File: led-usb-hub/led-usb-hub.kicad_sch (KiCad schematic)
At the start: 9 parts, among them J1 USB_C_Receptacle_USB2.0, U1 SL2.1A, Y1 12MHz

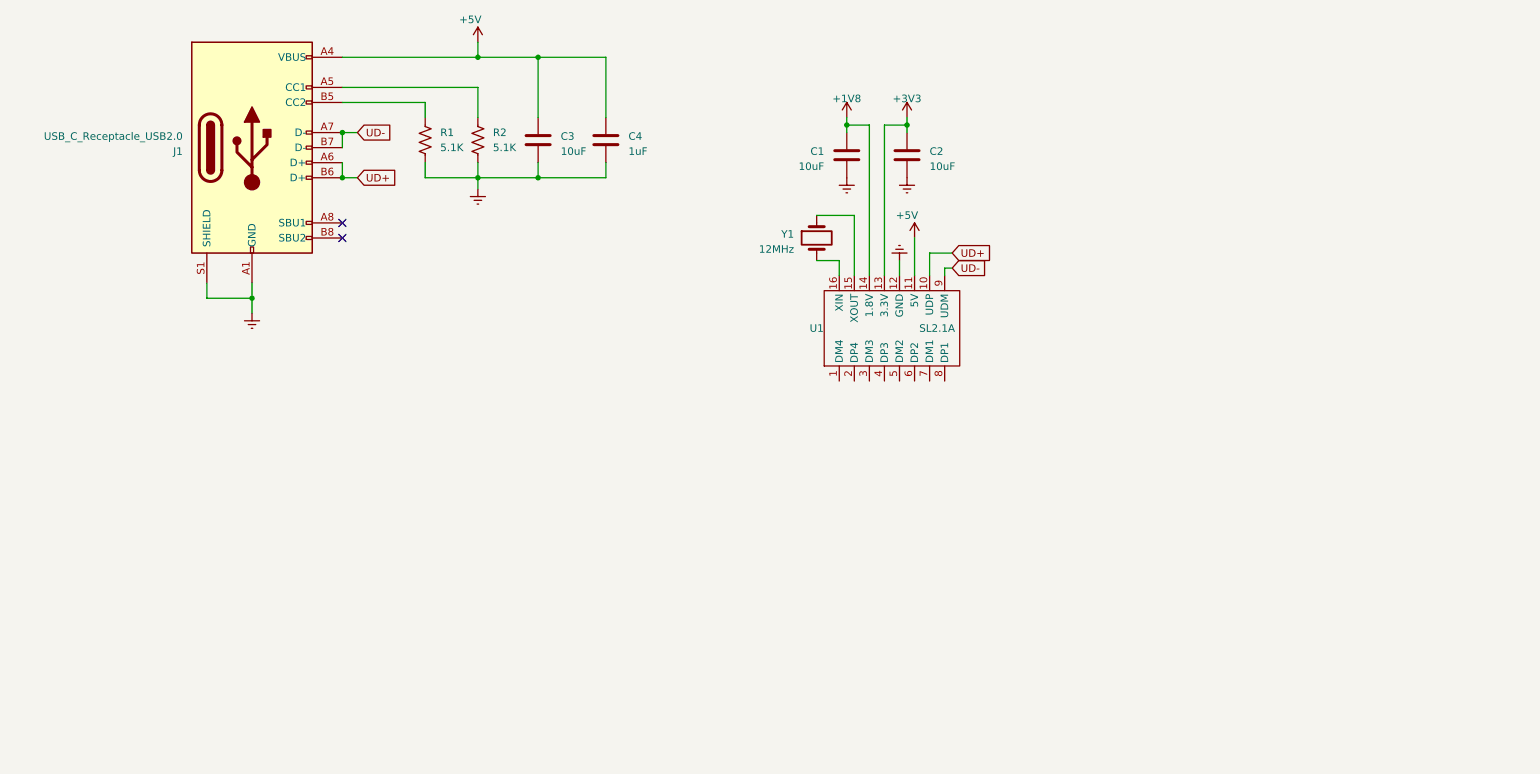
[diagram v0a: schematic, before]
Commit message: Added USB ports
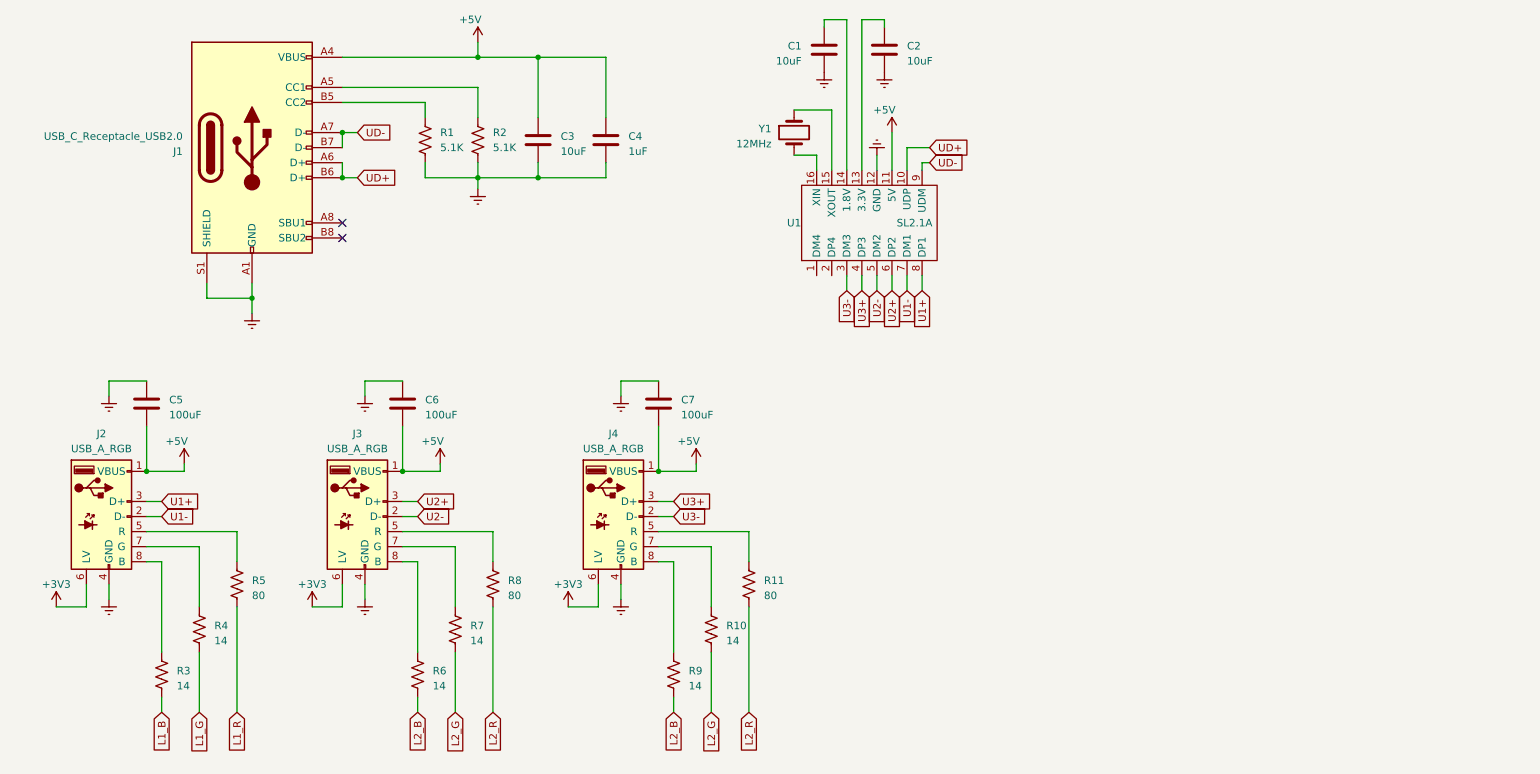
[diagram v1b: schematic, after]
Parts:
- added C5, C6, C7: 100uF, symbol Device:C
- added J2, J3, J4: USB_A_RGB, symbol Connector:USB_A_RGB
- added R10, R3, R4, R6, R7, R9: 14, symbol Device:R_US
- added R11, R5, R8: 80, symbol Device:R_US
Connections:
- net +3V3: now also J2.6 (LV), J3.6 (LV), J4.6 (LV); no longer C2.1, U1.13 (3.3V)
- net +5V: now also C5.2, C6.2, C7.2, J2.1 (VBUS), J3.1 (VBUS), J4.1 (VBUS)
- net Earth: now also C5.1, C6.1, C7.1, J2.4 (GND), J3.4 (GND), J4.4 (GND)
- net U3-: now reaches U1.3 (DM3)
- net U3-: now also J4.2 (D-)
- net U3+: now reaches U1.4 (DP3)
- net U3+: now also J4.3 (D+)
- net U2-: now reaches U1.5 (DM2)
- net U2-: now also J3.2 (D-)
- net U2+: now reaches U1.6 (DP2)
- net U2+: now also J3.3 (D+)
- net U1-: now reaches U1.7 (DM1)
- net U1-: now also J2.2 (D-)
- net U1+: now reaches U1.8 (DP1)
- net U1+: now also J2.3 (D+)
- net +1V8: no longer names the net of C1.1, U1.14 (1.8V)
- new net: J3.8 (B), R6.1
- new net: C2.1, U1.13 (3.3V)
- new net: J2.5 (R), R5.1
- new net: J2.7 (G), R4.1
- new net: J2.8 (B), R3.1
- new net: J3.7 (G), R7.1
- new net: J4.5 (R), R11.1
- new net: J4.8 (B), R9.1
- new net: J4.7 (G), R10.1
- new net: J3.5 (R), R8.1
- new net L1_B: R3.2
- new net L1_G: R4.2
- new net L1_R: R5.2
- new net L2_B: R6.2, R9.2
- new net L2_G: R10.2, R7.2
- new net L2_R: R11.2, R8.2
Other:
- moved on the sheet: C1, C2, U1, Y1

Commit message: Finish Schematic V1
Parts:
- added R12: 10k, symbol Device:R_US
- added SW1: SW_Push, symbol Switch:SW_Push
- added U2: KB2040, symbol MCU_RaspberryPi:KB2040
- C5: value 100uF -> 1uF
- C6, C7: value 100uF -> 100nF
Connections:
- net +5V: now also C5.1, C6.1, C7.1, U2.25 (RAW); no longer C5.2, C6.2, C7.2
- net Earth: now also C5.2, C6.2, C7.2, R12.2, SW1.2, U2.24 (GND), U2.4 (GND), U2.5 (GND); no longer C5.1, C6.1, C7.1
- net L1_B: now also U2.7 (D3)
- net L1_G: now also U2.3 (D1)
- net L1_R: now also U2.2 (D0)
- net L2_B: now also U2.10 (D6); no longer R9.2
- net L2_G: now also U2.9 (D5); no longer R10.2
- net L2_R: now also U2.8 (D4); no longer R11.2
- net U4-: now reaches U1.1 (DM4)
- net U4-: now also U2.26 (D-)
- net U4+: now reaches U1.2 (DP4)
- net U4+: now also U2.1 (D+)
- new net: SW1.1, U2.23 (RST)
- new net +3.3V: R12.1, U2.22 (3.3V)
- new net L3_B: R9.2, U2.13 (D9)
- new net L3_G: R10.2, U2.12 (D8)
- new net L3_R: R11.2, U2.11 (D7)
- no-connect marks 2 -> 11

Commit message: Create Footprints
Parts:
- C1, C2, C4, C5, C6, C7: footprint (none) -> Capacitor_SMD:C_0603_1608Metric_Pad1.08x0.95mm_HandSolder
- J1, SW1: footprint (none) -> Connector_USB:USB_C_Receptacle_GCT_USB4085
- J2, J3, J4: footprint (none) -> Connector_USB:USB_A_RGB
- R10, R11, R12, R3, R4, R5, R6, R7, R8, R9: footprint (none) -> Resistor_SMD:R_0603_1608Metric_Pad0.98x0.95mm_HandSolder
- U2: footprint (none) -> Module:KB2040
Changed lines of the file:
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@@
       (effects (font (size 1.27 1.27)) (justify left))
     )
-    (property "Footprint" "" (at 180.0352 44.45 0)
+    (property "Footprint" "Capacitor_SMD:C_0603_1608Metric_Pad1.08x0.95mm_HandSolder" (at 180.0352 44.45 0)
       (effects (font (size 1.27 1.27)) hide)
     )
@@
       (effects (font (size 1.27 1.27)))
     )
-    (property "Footprint" "" (at 195.58 114.3 0)
+    (property "Footprint" "Module:KB2040" (at 195.58 114.3 0)
       (effects (font (size 1.27 1.27)) hide)
     )
@@
       (effects (font (size 1.27 1.27)) (justify left))
     )
-    (property "Footprint" "" (at 81.026 128.524 90)
+    (property "Footprint" "Resistor_SMD:R_0603_1608Metric_Pad0.98x0.95mm_HandSolder" (at 81.026 128.524 90)
       (effects (font (size 1.27 1.27)) hide)
     )
@@
       (effects (font (size 1.27 1.27)) (justify left))
     )
-    (property "Footprint" "" (at 159.7152 26.67 0)
+    (property "Footprint" "Capacitor_SMD:C_0603_1608Metric_Pad1.08x0.95mm_HandSolder" (at 159.7152 26.67 0)
       (effects (font (size 1.27 1.27)) hide)
     )
@@
       (effects (font (size 1.27 1.27)))
     )
-    (property "Footprint" "" (at 30.48 104.14 0)
+    (property "Footprint" "Connector_USB:USB_A_RGB" (at 30.48 104.14 0)
       (effects (font (size 1.27 1.27)) hide)
     )
@@
       (effects (font (size 1.27 1.27)) (justify left))
     )
-    (property "Footprint" "" (at 50.546 113.284 90)
+    (property "Footprint" "Resistor_SMD:R_0603_1608Metric_Pad0.98x0.95mm_HandSolder" (at 50.546 113.284 90)
       (effects (font (size 1.27 1.27)) hide)
     )
@@
       (effects (font (size 1.27 1.27)) (justify left))
     )
-    (property "Footprint" "" (at 87.376 120.904 90)
+    (property "Footprint" "Resistor_SMD:R_0603_1608Metric_Pad0.98x0.95mm_HandSolder" (at 87.376 120.904 90)
       (effects (font (size 1.27 1.27)) hide)
     )
@@
       (effects (font (size 1.27 1.27)) (justify right))
     )
-    (property "Footprint" "" (at 55.88 39.37 0)
+    (property "Footprint" "Connector_USB:USB_C_Receptacle_GCT_USB4085" (at 55.88 39.37 0)
       (effects (font (size 1.27 1.27)) hide)
     )
@@
       (effects (font (size 1.27 1.27)) (justify left))
     )
-    (property "Footprint" "" (at 136.906 113.284 90)
+    (property "Footprint" "Resistor_SMD:R_0603_1608Metric_Pad0.98x0.95mm_HandSolder" (at 136.906 113.284 90)
       (effects (font (size 1.27 1.27)) hide)
     )
@@
       (effects (font (size 1.27 1.27)) (justify left))
     )
-    (property "Footprint" "" (at 112.7252 41.91 0)
+    (property "Footprint" "Capacitor_SMD:C_0603_1608Metric_Pad1.08x0.95mm_HandSolder" (at 112.7252 41.91 0)
       (effects (font (size 1.27 1.27)) hide)
     )
@@
       (effects (font (size 1.27 1.27)) (justify left))
     )
-    (property "Footprint" "" (at 227.0252 109.22 0)
+    (property "Footprint" "Capacitor_SMD:C_0603_1608Metric_Pad1.08x0.95mm_HandSolder" (at 227.0252 109.22 0)
       (effects (font (size 1.27 1.27)) hide)
     )
@@
       (effects (font (size 1.27 1.27)) (justify left))
     )
-    (property "Footprint" "" (at 124.206 128.524 90)
+    (property "Footprint" "Resistor_SMD:R_0603_1608Metric_Pad0.98x0.95mm_HandSolder" (at 124.206 128.524 90)
       (effects (font (size 1.27 1.27)) hide)
     )
@@
       (effects (font (size 1.27 1.27)) (justify left))
     )
-    (property "Footprint" "" (at 147.6248 26.67 0)
+    (property "Footprint" "Capacitor_SMD:C_0603_1608Metric_Pad1.08x0.95mm_HandSolder" (at 147.6248 26.67 0)
       (effects (font (size 1.27 1.27)) hide)
     )
@@
       (effects (font (size 1.27 1.27)) (justify left))
     )
-    (property "Footprint" "" (at 37.846 128.524 90)
+    (property "Footprint" "Resistor_SMD:R_0603_1608Metric_Pad0.98x0.95mm_HandSolder" (at 37.846 128.524 90)
       (effects (font (size 1.27 1.27)) hide)
     )
@@
       (effects (font (size 1.27 1.27)))
     )
-    (property "Footprint" "" (at 250.19 111.76 0)
+    (property "Footprint" "Connector_USB:USB_C_Receptacle_GCT_USB4085" (at 250.19 111.76 0)
       (effects (font (size 1.27 1.27)) hide)
     )
@@
       (effects (font (size 1.27 1.27)) (justify left))
     )
-    (property "Footprint" "" (at 240.9952 109.22 0)
+    (property "Footprint" "Capacitor_SMD:C_0603_1608Metric_Pad1.08x0.95mm_HandSolder" (at 240.9952 109.22 0)
       (effects (font (size 1.27 1.27)) hide)
     )
@@
       (effects (font (size 1.27 1.27)))
     )
-    (property "Footprint" "" (at 116.84 104.14 0)
+    (property "Footprint" "Connector_USB:USB_A_RGB" (at 116.84 104.14 0)
       (effects (font (size 1.27 1.27)) hide)
     )
@@
       (effects (font (size 1.27 1.27)))
     )
-    (property "Footprint" "" (at 73.66 104.14 0)
+    (property "Footprint" "Connector_USB:USB_A_RGB" (at 73.66 104.14 0)
       (effects (font (size 1.27 1.27)) hide)
     )
@@
       (effects (font (size 1.27 1.27)) (justify left))
     )
-    (property "Footprint" "" (at 44.196 120.904 90)
+    (property "Footprint" "Resistor_SMD:R_0603_1608Metric_Pad0.98x0.95mm_HandSolder" (at 44.196 120.904 90)
       (effects (font (size 1.27 1.27)) hide)
     )
@@
       (effects (font (size 1.27 1.27)) (justify left))
     )
-    (property "Footprint" "" (at 93.726 113.284 90)
+    (property "Footprint" "Resistor_SMD:R_0603_1608Metric_Pad0.98x0.95mm_HandSolder" (at 93.726 113.284 90)
       (effects (font (size 1.27 1.27)) hide)
     )
@@
       (effects (font (size 1.27 1.27)) (justify left))
     )
-    (property "Footprint" "" (at 130.556 120.904 90)
+    (property "Footprint" "Resistor_SMD:R_0603_1608Metric_Pad0.98x0.95mm_HandSolder" (at 130.556 120.904 90)
       (effects (font (size 1.27 1.27)) hide)
     )
@@
       (effects (font (size 1.27 1.27)) (justify left))
     )
-    (property "Footprint" "" (at 261.366 110.744 90)
-      (effects (font (size 1.27 1.27)) hide)
-    )
+    (property "Footprint" "Resistor_SMD:R_0603_1608Metric_Pad0.98x0.95mm_HandSolder" (at 261.366 110.744 90)
+      (effects (font (size 1.27 1.27)) hide)
+    )

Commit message: Start LAyout
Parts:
- SW1: footprint Connector_USB:USB_C_Receptacle_GCT_USB4085 -> (none)
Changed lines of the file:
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@@
       (effects (font (size 1.27 1.27)))
     )
-    (property "Footprint" "Connector_USB:USB_C_Receptacle_GCT_USB4085" (at 250.19 111.76 0)
+    (property "Footprint" "" (at 250.19 111.76 0)
       (effects (font (size 1.27 1.27)) hide)
     )

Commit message: Cont Routing, better layout
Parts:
- renumbered R9 to R11, R11 to R9
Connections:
- net +3.3V is gone; now on net +3V3: R12.1, U2.22 (3.3V)
- net L1_B: now also U2.2 (D0); no longer U2.7 (D3)
- net L1_R: now also U2.7 (D3); no longer U2.2 (D0)
- net L2_B: now also U2.8 (D4); no longer U2.10 (D6)
- net L2_R: now also U2.10 (D6); no longer U2.8 (D4)
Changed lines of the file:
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@@
     )
   )
-  (global_label "L2_R" (shape input) (at 175.26 116.84 180) (fields_autoplaced)
-    (effects (font (size 1.27 1.27)) (justify right))
-    (property "Intersheetrefs" "${INTERSHEET_REFS}" (at 167.879 116.84 0)
+  (global_label "L2_R" (shape input) (at 175.26 121.92 180) (fields_autoplaced)
+    (effects (font (size 1.27 1.27)) (justify right))
+    (property "Intersheetrefs" "${INTERSHEET_REFS}" (at 167.879 121.92 0)
       (effects (font (size 1.27 1.27)) (justify right) hide)
     )
@@
     )
   )
-  (global_label "L2_B" (shape input) (at 175.26 121.92 180) (fields_autoplaced)
-    (effects (font (size 1.27 1.27)) (justify right))
-    (property "Intersheetrefs" "${INTERSHEET_REFS}" (at 167.879 121.92 0)
-      (effects (font (size 1.27 1.27)) (justify right) hide)
-    )
-  )
-  (global_label "L1_R" (shape input) (at 175.26 101.6 180) (fields_autoplaced)
-    (effects (font (size 1.27 1.27)) (justify right))
-    (property "Intersheetrefs" "${INTERSHEET_REFS}" (at 167.879 101.6 0)
+  (global_label "L2_B" (shape input) (at 175.26 116.84 180) (fields_autoplaced)
+    (effects (font (size 1.27 1.27)) (justify right))
+    (property "Intersheetrefs" "${INTERSHEET_REFS}" (at 167.879 116.84 0)
+      (effects (font (size 1.27 1.27)) (justify right) hide)
+    )
+  )
+  (global_label "L1_R" (shape input) (at 175.26 114.3 180) (fields_autoplaced)
+    (effects (font (size 1.27 1.27)) (justify right))
+    (property "Intersheetrefs" "${INTERSHEET_REFS}" (at 167.879 114.3 0)
       (effects (font (size 1.27 1.27)) (justify right) hide)
     )
@@
     )
   )
-  (global_label "L1_B" (shape input) (at 175.26 114.3 180) (fields_autoplaced)
-    (effects (font (size 1.27 1.27)) (justify right))
-    (property "Intersheetrefs" "${INTERSHEET_REFS}" (at 167.879 114.3 0)
+  (global_label "L1_B" (shape input) (at 175.26 101.6 180) (fields_autoplaced)
+    (effects (font (size 1.27 1.27)) (justify right))
+    (property "Intersheetrefs" "${INTERSHEET_REFS}" (at 167.879 101.6 0)
       (effects (font (size 1.27 1.27)) (justify right) hide)
     )
@@
     )
   )
+  (symbol (lib_id "power:+3V3") (at 222.25 123.19 0) (mirror y) (unit 1)
+    (in_bom yes) (on_board yes) (dnp no)
+    (property "Reference" "#PWR01" (at 222.25 127 0)
+      (effects (font (size 1.27 1.27)) hide)
+    )
+    (property "Value" "+3V3" (at 222.25 119.38 0)
+      (effects (font (size 1.27 1.27)))
+    )
+    (property "Footprint" "" (at 222.25 123.19 0)
+      (effects (font (size 1.27 1.27)) hide)
+    )
+    (property "Datasheet" "" (at 222.25 123.19 0)
+      (effects (font (size 1.27 1.27)) hide)
+    )
+    (pin "1")
+    (instances
+      (project "led-usb-hub"
+        (path "/872229b5-49ea-4e15-b82a-ed1f213c1d75"
+          (reference "#PWR01") (unit 1)
+        )
+      )
+    )
+  )
   (symbol (lib_id "Device:C") (at 179.07 40.64 0) (unit 1)
     (in_bom yes) (on_board yes) (dnp no)
@@
         (path "/872229b5-49ea-4e15-b82a-ed1f213c1d75"
           (reference "#PWR025") (unit 1)
-        )
-      )
-    )
-  )
-  (symbol (lib_id "power:+3.3V") (at 222.25 123.19 0) (unit 1)
-    (in_bom yes) (on_board yes) (dnp no) (fields_autoplaced)
-    (property "Reference" "#PWR024" (at 222.25 127 0)
-      (effects (font (size 1.27 1.27)) hide)
-    )
-    (property "Value" "+3.3V" (at 222.25 119.38 0)
-      (effects (font (size 1.27 1.27)))
-    )
-    (property "Footprint" "" (at 222.25 123.19 0)
-      (effects (font (size 1.27 1.27)) hide)
-    )
-    (property "Datasheet" "" (at 222.25 123.19 0)
-      (effects (font (size 1.27 1.27)) hide)
-    )
-    (pin "1")
-    (instances
-      (project "led-usb-hub"
-        (path "/872229b5-49ea-4e15-b82a-ed1f213c1d75"
-          (reference "#PWR024") (unit 1)
         )
       )
@@
     )
   )
+  (symbol (lib_id "power:+3V3") (at 260.35 104.14 0) (mirror y) (unit 1)
+    (in_bom yes) (on_board yes) (dnp no)
+    (property "Reference" "#PWR013" (at 260.35 107.95 0)
+      (effects (font (size 1.27 1.27)) hide)
+    )
+    (property "Value" "+3V3" (at 260.35 100.33 0)
+      (effects (font (size 1.27 1.27)))
+    )
+    (property "Footprint" "" (at 260.35 104.14 0)
+      (effects (font (size 1.27 1.27)) hide)
+    )
+    (property "Datasheet" "" (at 260.35 104.14 0)
+      (effects (font (size 1.27 1.27)) hide)
+    )
+    (pin "1")
+    (instances
+      (project "led-usb-hub"
+        (path "/872229b5-49ea-4e15-b82a-ed1f213c1d75"
+          (reference "#PWR013") (unit 1)
+        )
+      )
+    )
+  )
   (symbol (lib_id "power:Earth") (at 148.59 26.67 0) (unit 1)
     (in_bom yes) (on_board yes) (dnp no) (fields_autoplaced)
@@
   (symbol (lib_id "Device:R_US") (at 135.89 113.03 0) (unit 1)
     (in_bom yes) (on_board yes) (dnp no) (fields_autoplaced)
-    (property "Reference" "R11" (at 138.43 112.395 0)
+    (property "Reference" "R9" (at 138.43 112.395 0)
       (effects (font (size 1.27 1.27)) (justify left))
     )
@@
       (project "led-usb-hub"
         (path "/872229b5-49ea-4e15-b82a-ed1f213c1d75"
-          (reference "R11") (unit 1)
+          (reference "R9") (unit 1)
         )
       )
@@
   (symbol (lib_id "Device:R_US") (at 123.19 128.27 0) (unit 1)
     (in_bom yes) (on_board yes) (dnp no) (fields_autoplaced)
-    (property "Reference" "R9" (at 125.73 127.635 0)
+    (property "Reference" "R11" (at 125.73 127.635 0)
       (effects (font (size 1.27 1.27)) (justify left))
     )
@@
       (project "led-usb-hub"
         (path "/872229b5-49ea-4e15-b82a-ed1f213c1d75"
-          (reference "R9") (unit 1)
+          (reference "R11") (unit 1)
         )
       )
@@
         )
       )
-    )
-  )
-  (symbol (lib_id "power:+3.3V") (at 260.35 104.14 0) (unit 1)
-    (in_bom yes) (on_board yes) (dnp no) (fields_autoplaced)
-    (property "Reference" "#PWR023" (at 260.35 107.95 0)
-      (effects (font (size 1.27 1.27)) hide)
-    )
-    (property "Value" "+3.3V" (at 260.35 100.33 0)
-      (effects (font (size 1.27 1.27)))
-    )
-    (property "Footprint" "" (at 260.35 104.14 0)
-      (effects (font (size 1.27 1.27)) hide)
-    )
-    (property "Datasheet" "" (at 260.35 104.14 0)
-      (effects (font (size 1.27 1.27)) hide)
-    )
-    (pin "1")
-    (instances
-      (project "led-usb-hub"
-        (path "/872229b5-49ea-4e15-b82a-ed1f213c1d75"
-          (reference "#PWR023") (unit 1)
-        )
-      )

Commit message: finish routing NEED: graphics and labels
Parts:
- added C8, C9: 8pF, Capacitor_SMD:C_0603_1608Metric_Pad1.08x0.95mm_HandSolder, symbol Device:C
- SW1: footprint (none) -> kss_switch:SW_KSS241GLFS_CNK
- Y1: footprint (none) -> ecs_osc:XTAL_ECS-120-8-33-JGN-TR3
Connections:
- net Earth: now also SW1.1, Y1.2 (GND), Y1.4 (GND), C8.2, C9.2; no longer SW1.2
- net at U2.23 (RST): now also SW1.2; no longer SW1.1
- net X+: now reaches U1.15 (XOUT)
- net X+: now also Y1.3, C8.1; no longer Y1.1
- net X-: now reaches U1.16 (XIN)
- net X-: now also Y1.1, C9.1; no longer Y1.2
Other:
- moved on the sheet: C1, C2, C7, U1
